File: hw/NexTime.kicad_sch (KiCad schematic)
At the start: 74 parts, among them J101 CR2032, J102 pwr+data, U101 SRV05-4, U102 XTAA5212IRGER, U103 ESP32-S3-WROOM-1-N8R8, U104 OPA4863, U105 LMR51430YDDCR, U106 TPS74633PQWDRBRQ1, Y101 RV-3032-C7_32.768kHz-2.5PPM-T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

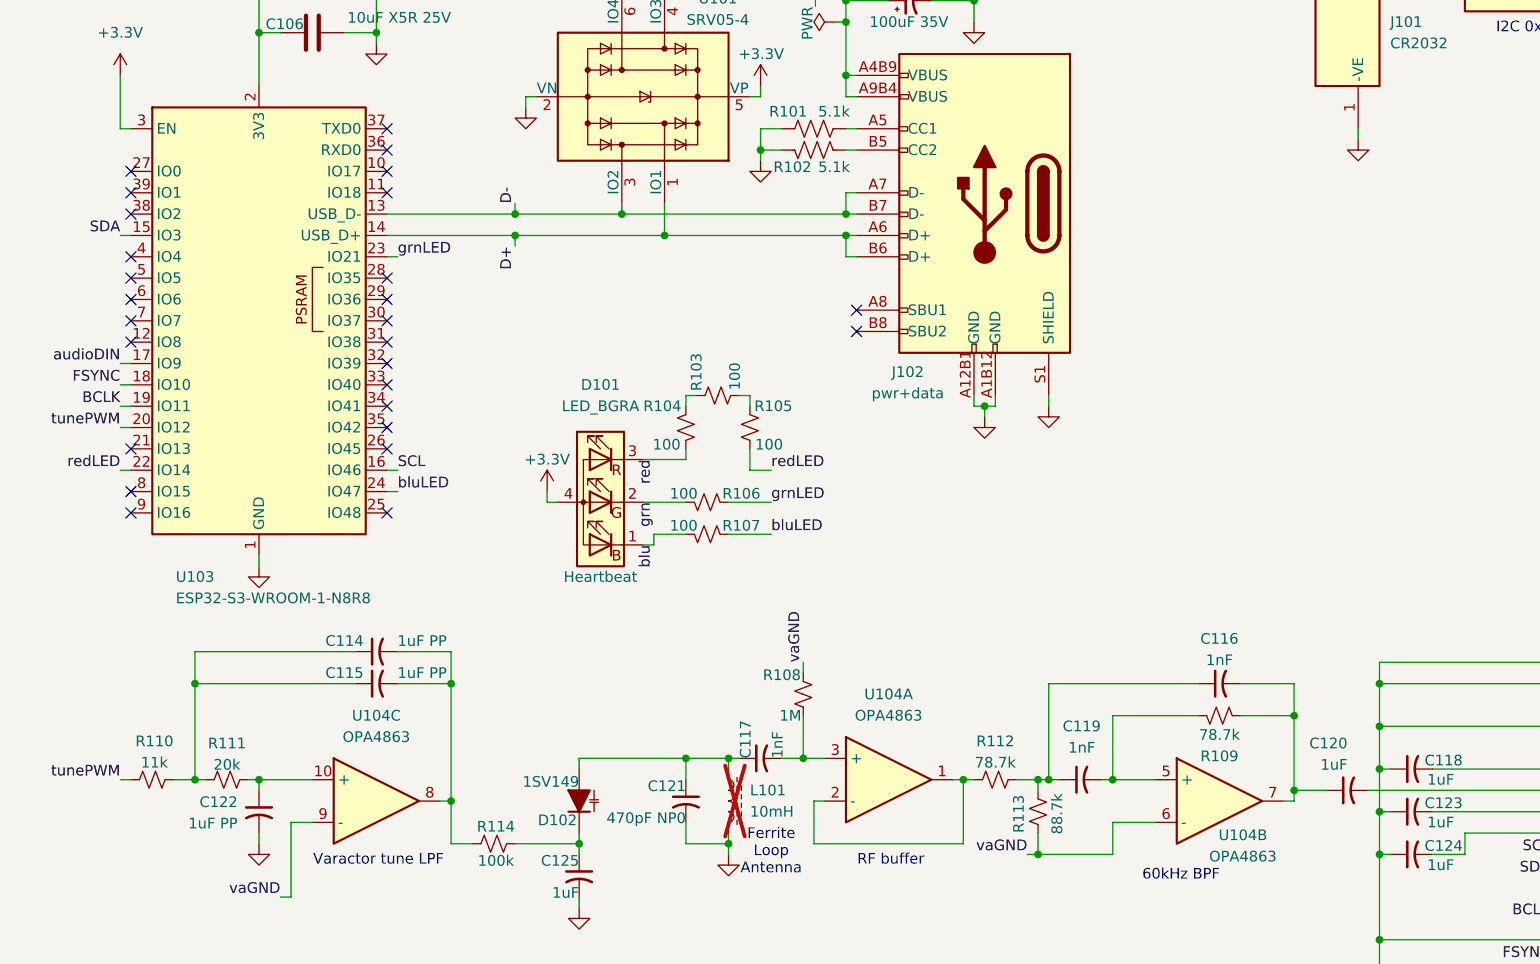
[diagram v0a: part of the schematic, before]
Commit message: Added RECOVER pushbutton. Cleared the way for display but not added yet.
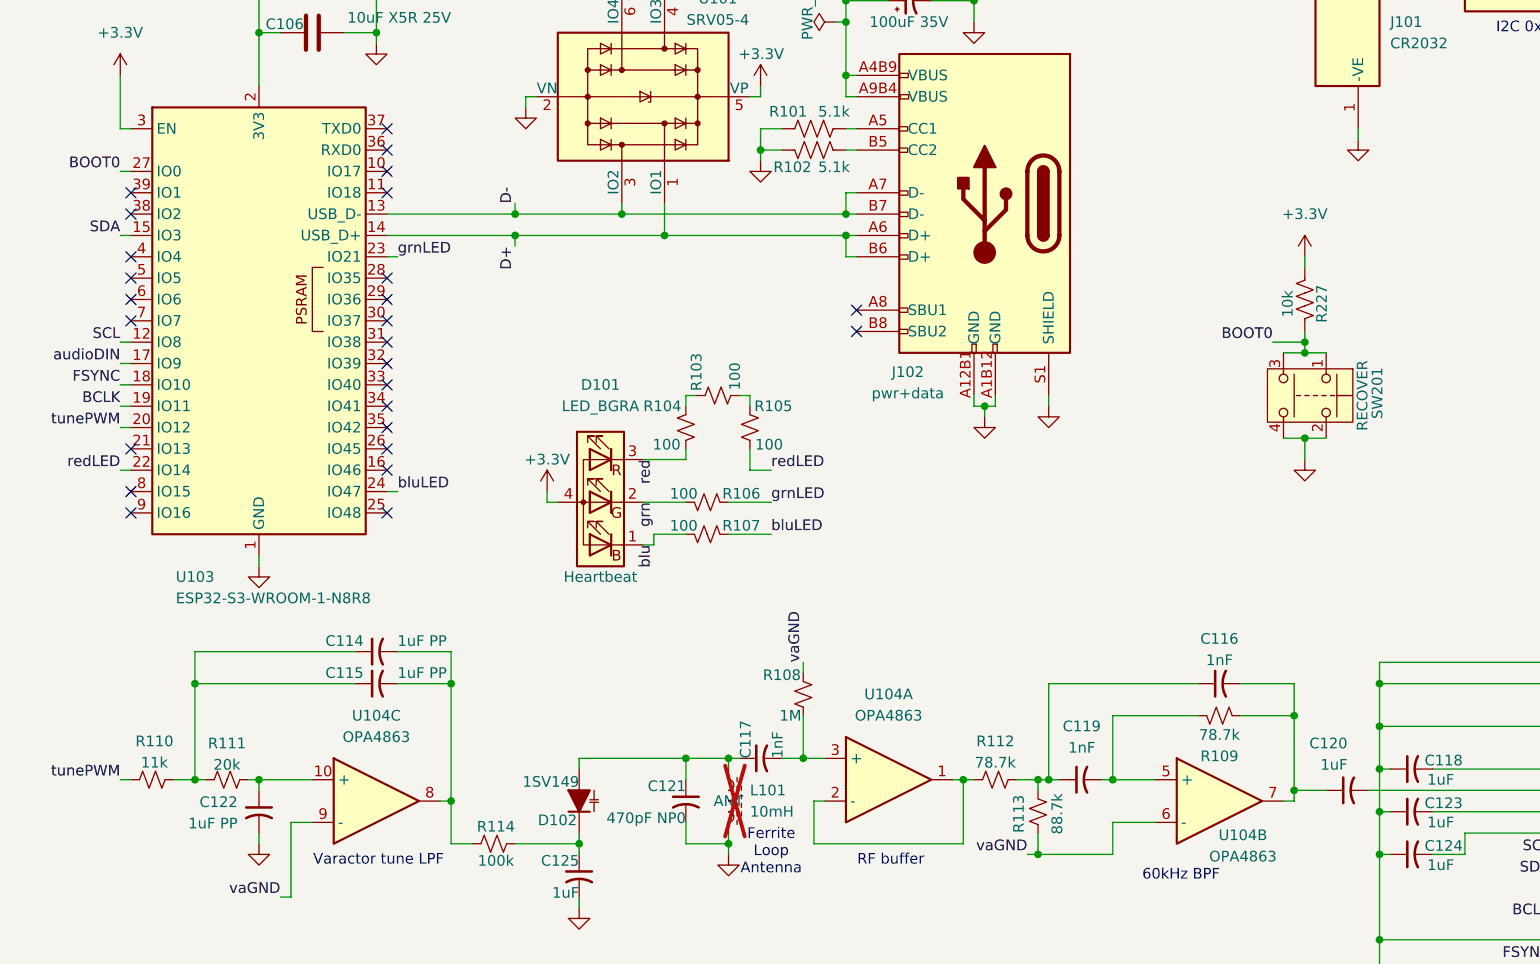
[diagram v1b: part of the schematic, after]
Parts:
- added R227: 10k, Resistor_SMD:R_0402_1005Metric, symbol Device:R_US
- added SW201: Push button switch, Library:EVQPUC02K, symbol Switch:SW_Push_Dual
- L101: label (none) -> ANT
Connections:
- net +3.3V: now also R227.1
- net GND: now also SW201.2, SW201.4
- net SCL: now also U103.12 (IO8); no longer U103.16 (IO46)
- net BOOT0: now reaches U103.27 (IO0)
- net BOOT0: now also R227.2, SW201.1, SW201.3
- no-connect marks 40 -> 39

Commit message: Update 3d models for parts. Display conn still missing
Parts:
- added C106: 10uF, Capacitor_SMD:C_0402_1005Metric, symbol Device:C_Small_US
- added C107, C115: 100nF, Capacitor_SMD:C_0402_1005Metric, symbol Device:C_Small_US
- added J101: ER-CON40HB-2, Library:ER-CON40HB-2, symbol Connector_Generic:Conn_01x40
- renumbered C106 to C105, C107 to C108, C108 to C109, C109 to C110, C110 to C111, C111 to C112, C112 to C113, C113 to C114, C105 to C116, C116 to C117, C114 to C118, C115 to C119, C117 to C120, C118 to C121, C119 to C122, C120 to C123, C121 to C124, C122 to C125, C123 to C126, C124 to C127, C125 to C128, C126 to C129, C127 to C130, C128 to C131, C129 to C132, C130 to C133, C131 to C134, C132 to C135, C133 to C136, C134 to C137, D102 to D101, D101 to D102, J101 to J103, R115 to R103, R116 to R104, R108 to R105, R109 to R106, R227 to R107, R110 to R108, R111 to R109, R112 to R110, R113 to R111, R114 to R112, R103 to R113, R104 to R114, R105 to R115, R106 to R116, R107 to R118, R118 to R119, R119 to R120, R120 to R121, SW201 to SW101
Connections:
- net +3.3V: now also C106.1, C107.1, J101.2 (Pin_2)
- net GND: now also C106.2, C107.2, C115.2, J101.1 (Pin_1), J101.40 (Pin_40)
- net at J103.2, J103.3, Y101.1 (VBACKUP): now also C115.1
- net dispNRD: now reaches U103.10 (IO17)
- net dispNRD: now also J101.5 (Pin_5)
- net dispNWR: now reaches U103.11 (IO18)
- net dispNWR: now also J101.6 (Pin_6)
- net blPWM: now reaches U103.21 (IO13)
- net blPWM: now also J101.39 (Pin_39)
- net dispD6: now reaches U103.25 (IO48)
- net dispD6: now also J101.15 (Pin_15)
- net dispD5: now reaches U103.26 (IO45)
- net dispD5: now also J101.14 (Pin_14)
- net dispD0: now reaches U103.31 (IO38)
- net dispD0: now also J101.9 (Pin_9)
- net dispD1: now reaches U103.32 (IO39)
- net dispD1: now also J101.10 (Pin_10)
- net dispD2: now reaches U103.33 (IO40)
- net dispD2: now also J101.11 (Pin_11)
- net dispD3: now reaches U103.34 (IO41)
- net dispD3: now also J101.12 (Pin_12)
- net dispD4: now reaches U103.35 (IO42)
- net dispD4: now also J101.13 (Pin_13)
- net dispD7: now reaches U103.38 (IO2)
- net dispD7: now also J101.16 (Pin_16)
- net dispDC: now reaches U103.4 (IO4)
- net dispDC: now also J101.4 (Pin_4)
- net dispNCS: now reaches U103.5 (IO5)
- net dispNCS: now also J101.3 (Pin_3)
- net dispBUSY: now reaches U103.6 (IO6)
- net dispBUSY: now also J101.37 (Pin_37)
- net dispTE: now reaches U103.7 (IO7)
- net dispTE: now also J101.8 (Pin_8)
- net dispNRST: now reaches U103.8 (IO15)
- net dispNRST: now also J101.7 (Pin_7)
- net bluLED renamed bluHB
- net grnLED renamed grnHB
- net redLED renamed redHB
- no-connect marks 39 -> 44
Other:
- moved on the sheet: C101, C102, C104, C108, C109, C110, C111, C112, C113, C114, C116, C117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

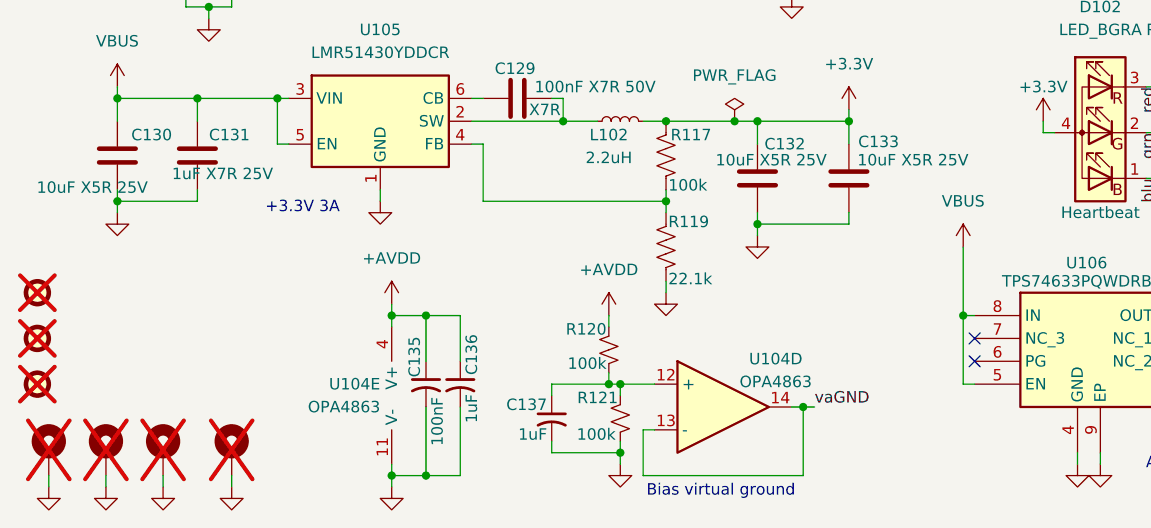
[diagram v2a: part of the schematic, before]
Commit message: Improve power routing
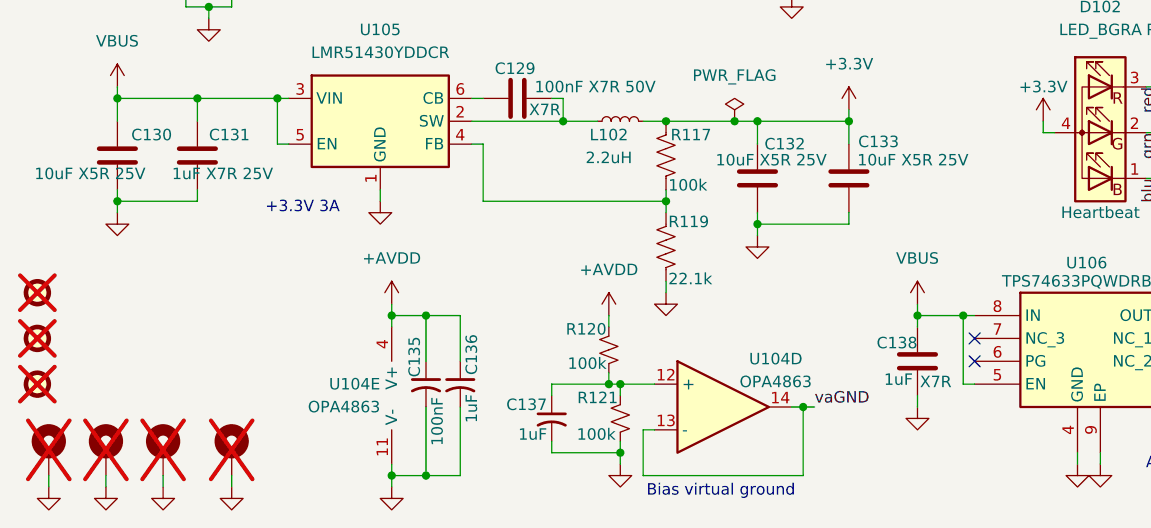
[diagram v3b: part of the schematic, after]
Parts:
- added C138: 1uF, Capacitor_SMD:C_0402_1005Metric, symbol Device:C
- C114, C121, C123, C126, C127, C128, C136, C137: MFG (none) -> muRata; MPN (none) -> GRM155Z71A105KE1D; Mouser_PN (none) -> 81-GRM155Z71A105KE1D; cap-type (none) -> X7R; working-voltage (none) -> 10V
- R112, R120, R121: MFG (none) -> Bourns; MPN (none) -> CRT0402-FZ-1003GLF; Mouser_PN (none) -> 652-CRT0402FZ1003GLF
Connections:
- net GND: now also C138.2
- net VBUS: now also C138.1

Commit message: Move things around to make room for FLAT CR2032 bat holder. Add RF shield ring around high Z sensitivity circuitry. Shove display connector toward board left and move RECOVER button up on top by display connector. Move temp sensitive RTC away from heat producing components.
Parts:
- removed J103: CR2032, Library:S8401-46, symbol Library:S8401-46
- added BT101: CR2032, Battery:BatteryHolder_Keystone_3034_1x20mm, symbol Device:Battery_Cell
- C117, C122: value 1nF -> 1nF NP0
- C118, C119, C125: value 1uF PP -> 100nF NP0; footprint Library:R82DC4100AA60K -> Capacitor_SMD:C_1206_3216Metric
- R106: value 78.7k -> 42.1k
- R108: value 11k -> 110k
- R109: value 20k -> 200k
- R110: value 78.7k -> 21k
- R111: value 88.7k -> 169
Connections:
- net GND: now also R111.1, BT101.2 (-)
- net vaGND: now also U104.5 (+); no longer R111.1, U104.6 (-)
- net at C115.1, Y101.1 (VBACKUP): now also BT101.1 (+)
- net at C122.2, R106.1: now also U104.6 (-); no longer U104.5 (+)
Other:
- moved on the sheet: R111
